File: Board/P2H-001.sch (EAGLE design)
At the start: 28 parts, among them IC1 LTC485N, IC2 74LS07N, IC3 74LS157N, IC4 LTC485N, IC5 TLC5941NT, IC6 TLC5941NT, U1 ARDUINO_PRO_MINI

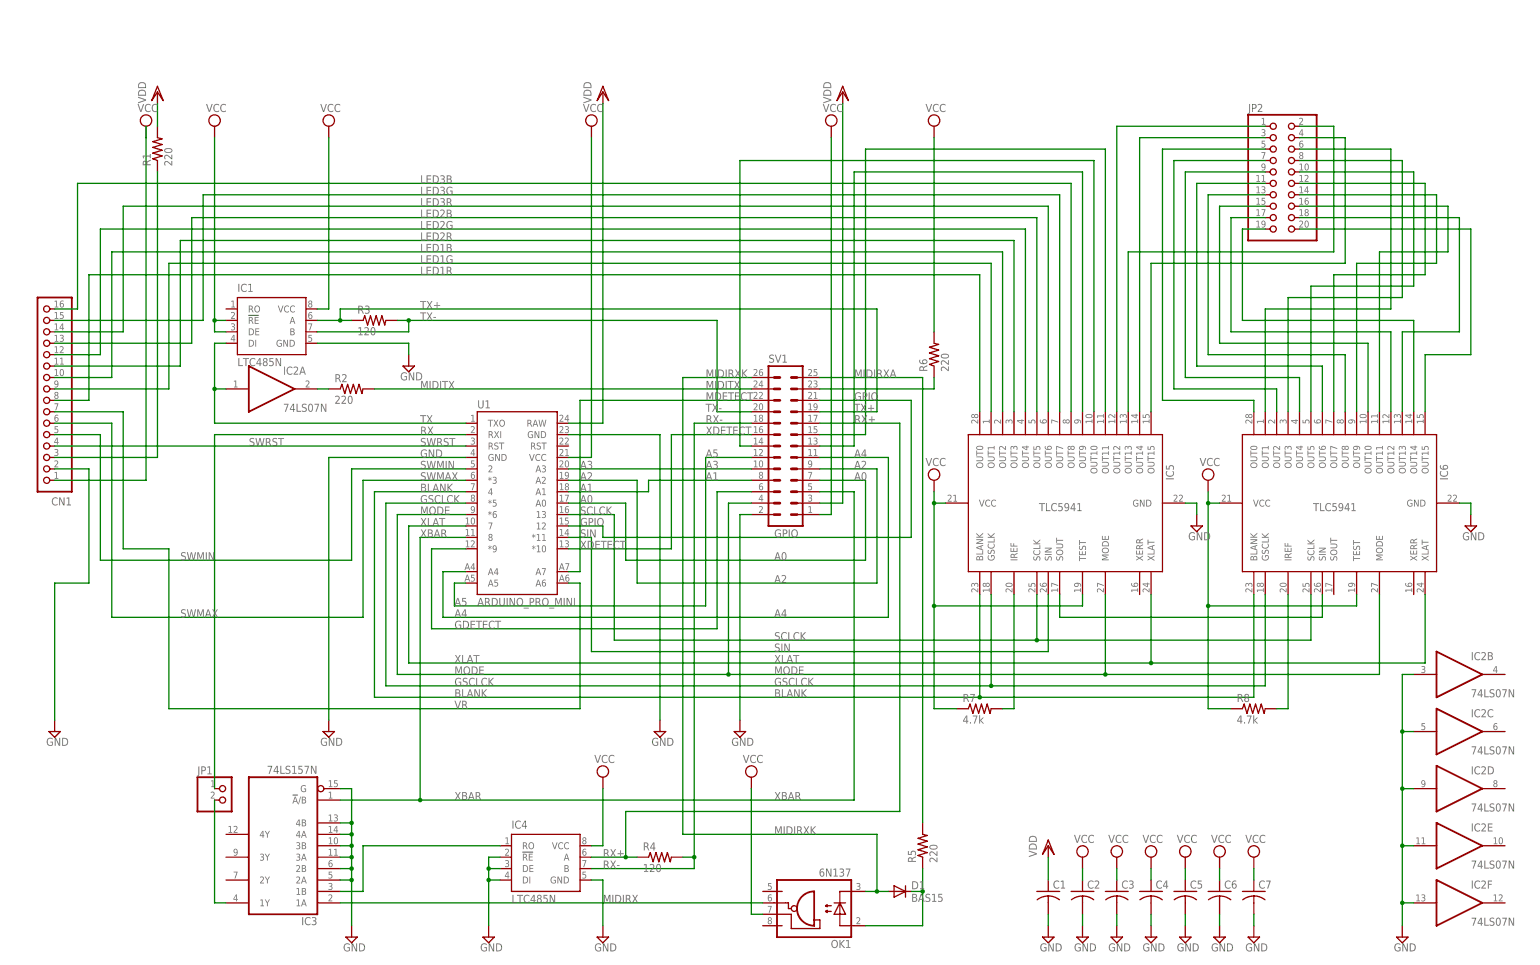
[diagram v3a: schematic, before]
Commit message: fixed wiring.
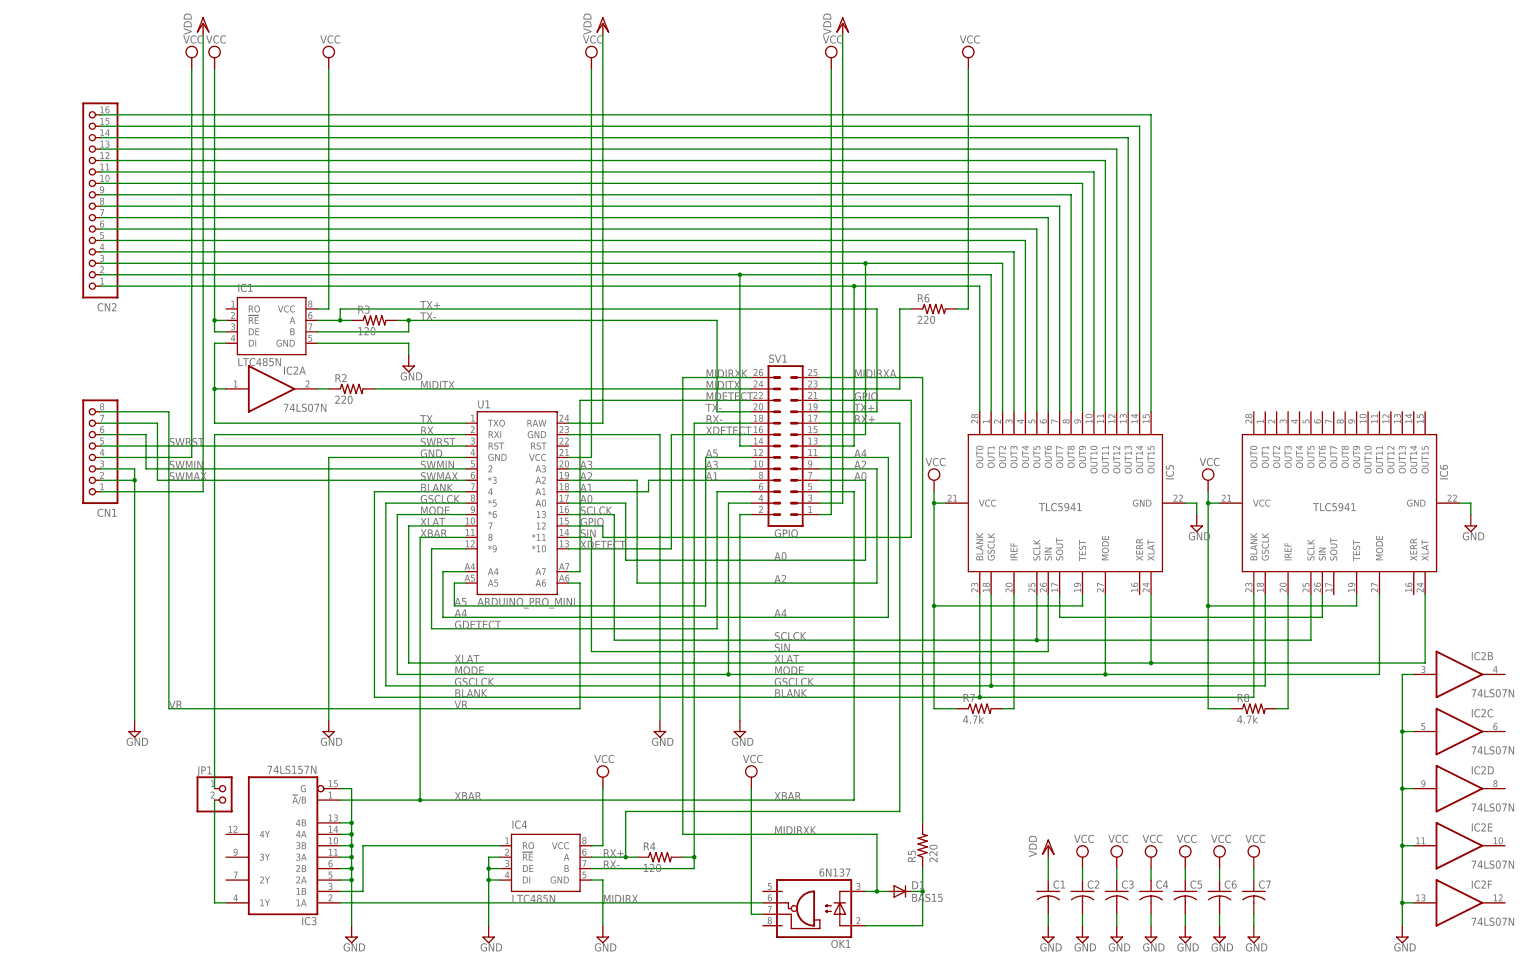
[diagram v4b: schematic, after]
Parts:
- removed JP2: (no value), pinhead:PINHD-2X10
- removed R1: 220, resistor:R-US_0204/5
- added CN2: (no value), jst-ph:S16B-PH-K-S
- CN1: device jst-ph:S16B-PH-K-S -> jst-ph:S8B-PH-K-S
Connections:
- removed net LED1B: CN1.10, IC5.OUT2
- removed net LED1G: CN1.9, IC5.OUT1
- removed net LED1R: CN1.8, IC5.OUT0
- removed net LED2R: CN1.11, IC5.OUT3
- removed net N$26: IC6.OUT0, JP2.5
- removed net N$27: IC6.OUT2, JP2.7
- removed net N$28: IC6.OUT4, JP2.9
- removed net N$29: IC6.OUT6, JP2.11
- removed net N$30: IC6.OUT8, JP2.13
- removed net N$31: IC6.OUT10, JP2.15
- removed net N$32: IC6.OUT12, JP2.17
- removed net N$33: IC6.OUT14, JP2.19
- removed net N$34: IC6.OUT1, JP2.6
- removed net N$35: IC6.OUT3, JP2.8
- removed net N$36: IC6.OUT5, JP2.10
- removed net N$39: IC6.OUT7, JP2.12
- removed net N$40: IC6.OUT9, JP2.14
- removed net N$41: IC6.OUT11, JP2.16
- removed net N$42: IC6.OUT13, JP2.18
- removed net N$43: IC6.OUT15, JP2.20
- new net N$6: CN2.10, IC5.OUT9
- new net N$8: CN2.12, IC5.OUT11
- new net N$9: CN2.4, IC5.OUT3
- net GND: now also CN1.3
- net LED2B: now also CN2.6; no longer CN1.13
- net LED2G: now also CN2.5; no longer CN1.12
- net LED3B: now also CN2.9; no longer CN1.16
- net LED3G: now also CN2.8; no longer CN1.15
- net LED3R: now also CN2.7; no longer CN1.14
- net LEDA: now also CN2.1, IC5.OUT0; no longer IC5.OUT9
- net N$12: now also CN2.2, IC5.OUT1; no longer IC5.OUT10
- net N$14: now also CN2.3, IC5.OUT2; no longer IC5.OUT11
- net N$24: now also CN2.15; no longer JP2.3
- net N$25: now also CN2.16; no longer JP2.4
- net N$3: now also CN2.13; no longer JP2.1
- net N$5: now also CN2.14; no longer JP2.2
- net N$7: now also CN2.11, IC5.OUT10; no longer CN1.3, R1.1
- net SWMAX: now also CN1.7; no longer CN1.6
- net SWMIN: now also CN1.6; no longer CN1.5
- net SWRST: now also CN1.5; no longer CN1.4
- net VCC: now also CN1.4; no longer CN1.1
- net VDD: now also CN1.1; no longer R1.2
- net VR: now also CN1.8; no longer CN1.7
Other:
- moved on the sheet: R6

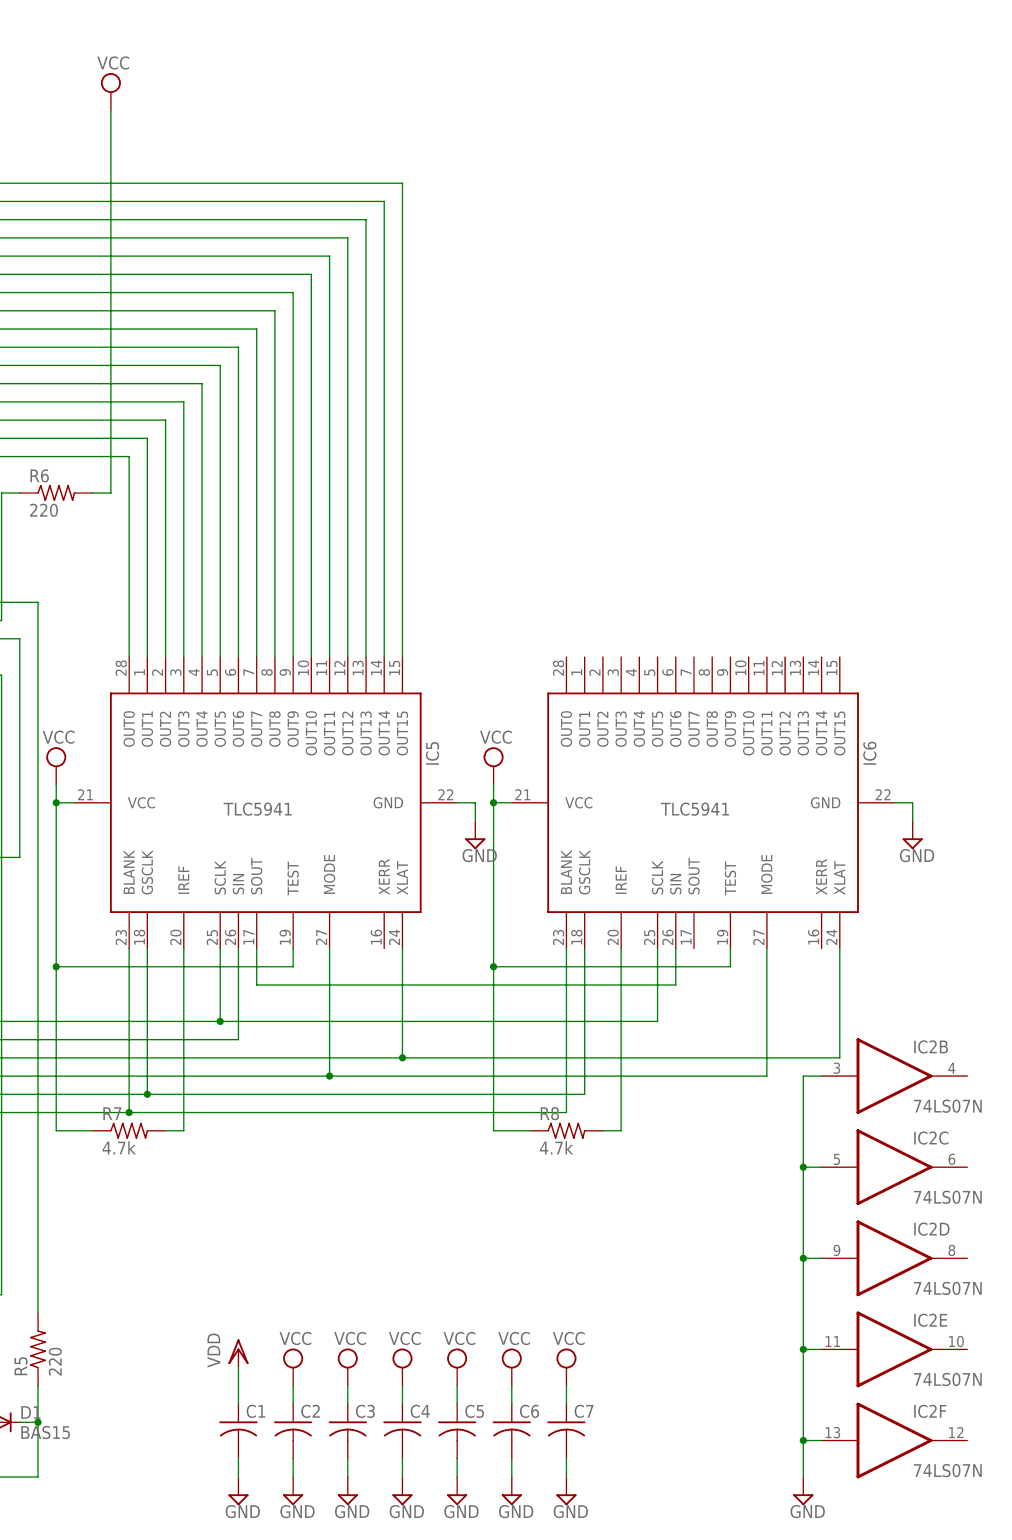
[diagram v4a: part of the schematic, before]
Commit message: One TLC.
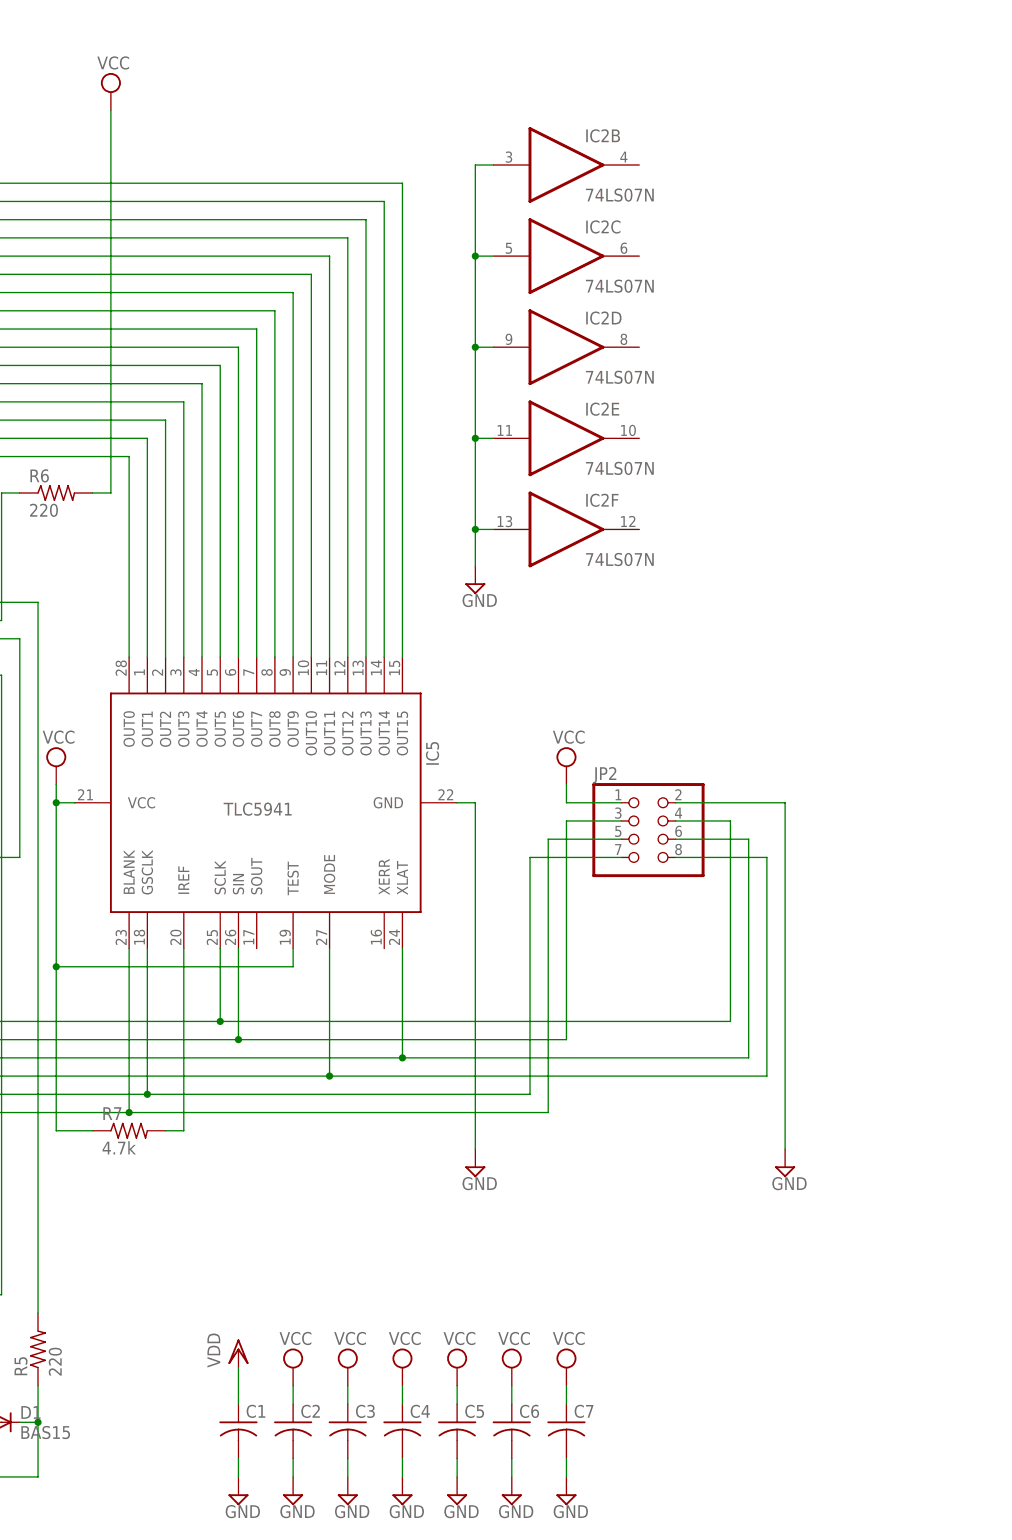
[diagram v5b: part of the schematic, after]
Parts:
- removed IC6: TLC5941NT, adafruit:TLC5941NT
- removed R8: 4.7k, resistor:R-US_0204/5
- added JP2: (no value), pinhead:PINHD-2X4
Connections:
- removed net N$16: IC5.SOUT, IC6.SIN
- removed net N$38: IC6.IREF, R8.2
- net BLANK: now also JP2.5; no longer IC6.BLANK
- net GND: now also JP2.2; no longer IC6.GND
- net GSCLCK: now also JP2.7; no longer IC6.GSCLK
- net MODE: now also JP2.8; no longer IC6.MODE
- net SCLCK: now also JP2.4; no longer IC6.SCLK
- net SIN: now also JP2.3
- net VCC: now also JP2.1; no longer IC6.TEST, IC6.VCC, R8.1
- net XLAT: now also JP2.6; no longer IC6.XLAT
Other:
- moved on the sheet: IC2B, IC2C, IC2D, IC2E, IC2F

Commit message: Label.
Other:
- note added: "Pineapple II Hydrogen 0.1.1 Copyright 2015 by Pineapple.cc"
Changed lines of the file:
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@@
 <setting verticaltext="up"/>
 </settings>
-<grid distance="0.1" unitdist="inch" unit="inch" style="lines" multiple="1" display="yes" altdistance="0.01" altunitdist="inch" altunit="inch"/>
+<grid distance="0.1" unitdist="inch" unit="inch" style="lines" multiple="1" display="no" altdistance="0.01" altunitdist="inch" altunit="inch"/>
 <layers>
 <layer number="1" name="Top" color="4" fill="1" visible="no" active="no"/>
@@
 <sheet>
 <plain>
+<text x="276.86" y="-71.12" size="1.778" layer="91">Pineapple II Hydrogen 0.1.1
+Copyright 2015 by Pineapple.cc</text>
 </plain>
 <instances>
@@
 </schematic>
 </drawing>
+<compatibility>
+<note version="6.3" minversion="6.2.2" severity="warning">
+Since Version 6.2.2 text objects can contain more than one line,
+which will not be processed correctly with this version.
+</note>
+</compatibility>
 </eagle>
